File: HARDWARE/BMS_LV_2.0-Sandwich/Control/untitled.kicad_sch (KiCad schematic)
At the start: 14 parts, among them IC2 M24M02E-UFMN6TP, U1 STM32G484RETx, Y1 ATX-11-F-32.000MHZ-F05-T

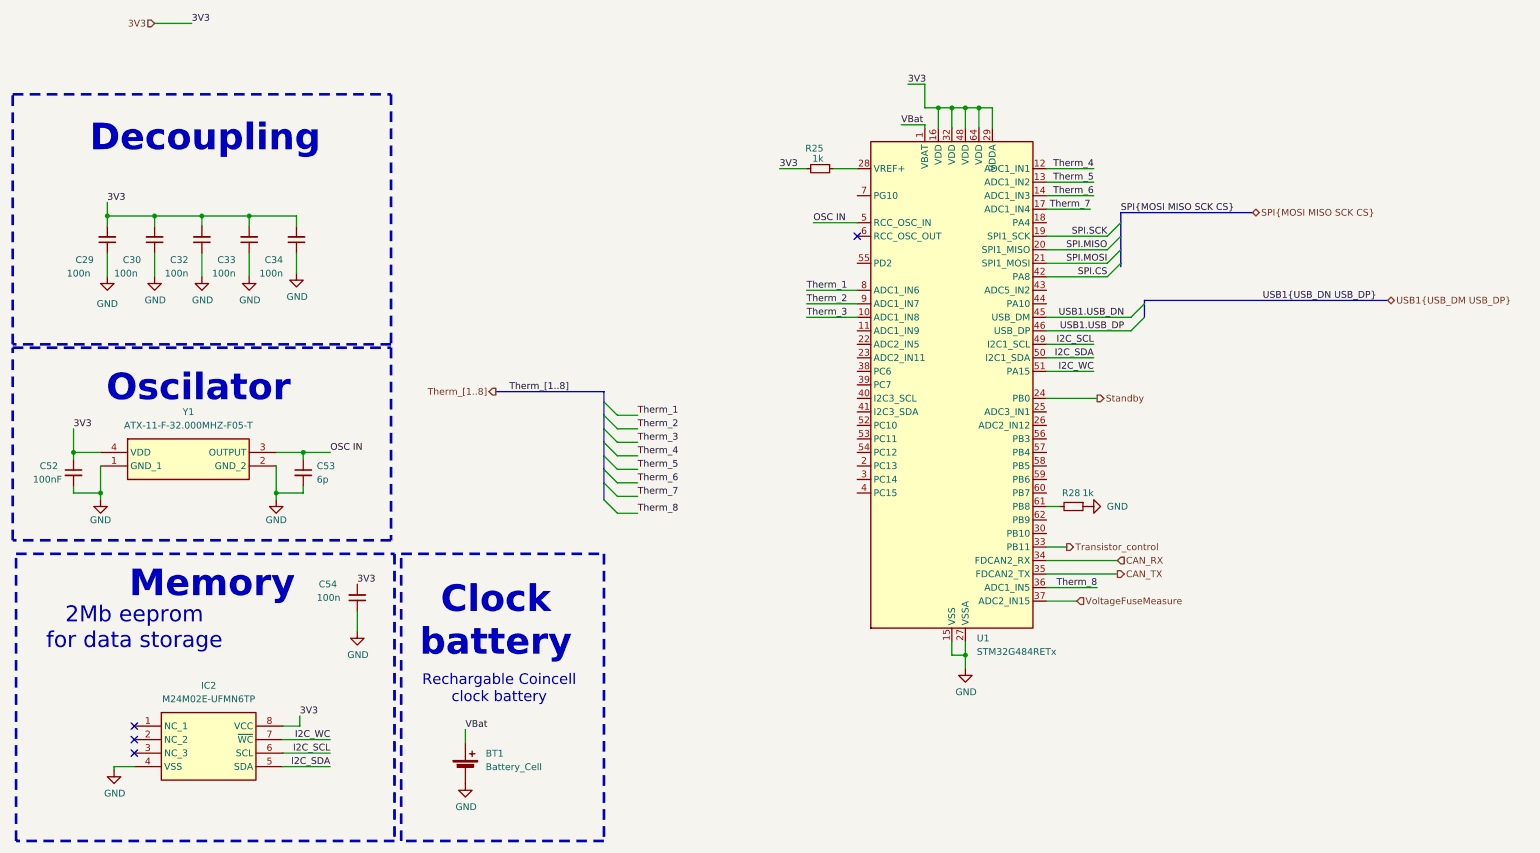
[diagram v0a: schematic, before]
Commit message: Zmiany w power: nowe bezpieczniki, nowy wymienialny layout dla tych bezpiecznikow, dodano diode zenera dla stabilizacji napięcia, zmiany dla control:  wyjebany eeprom, przesunięty can, zmieniony layout przetwornic, dodano programator i tvs, jeszcze do dokonczenia routing w control.
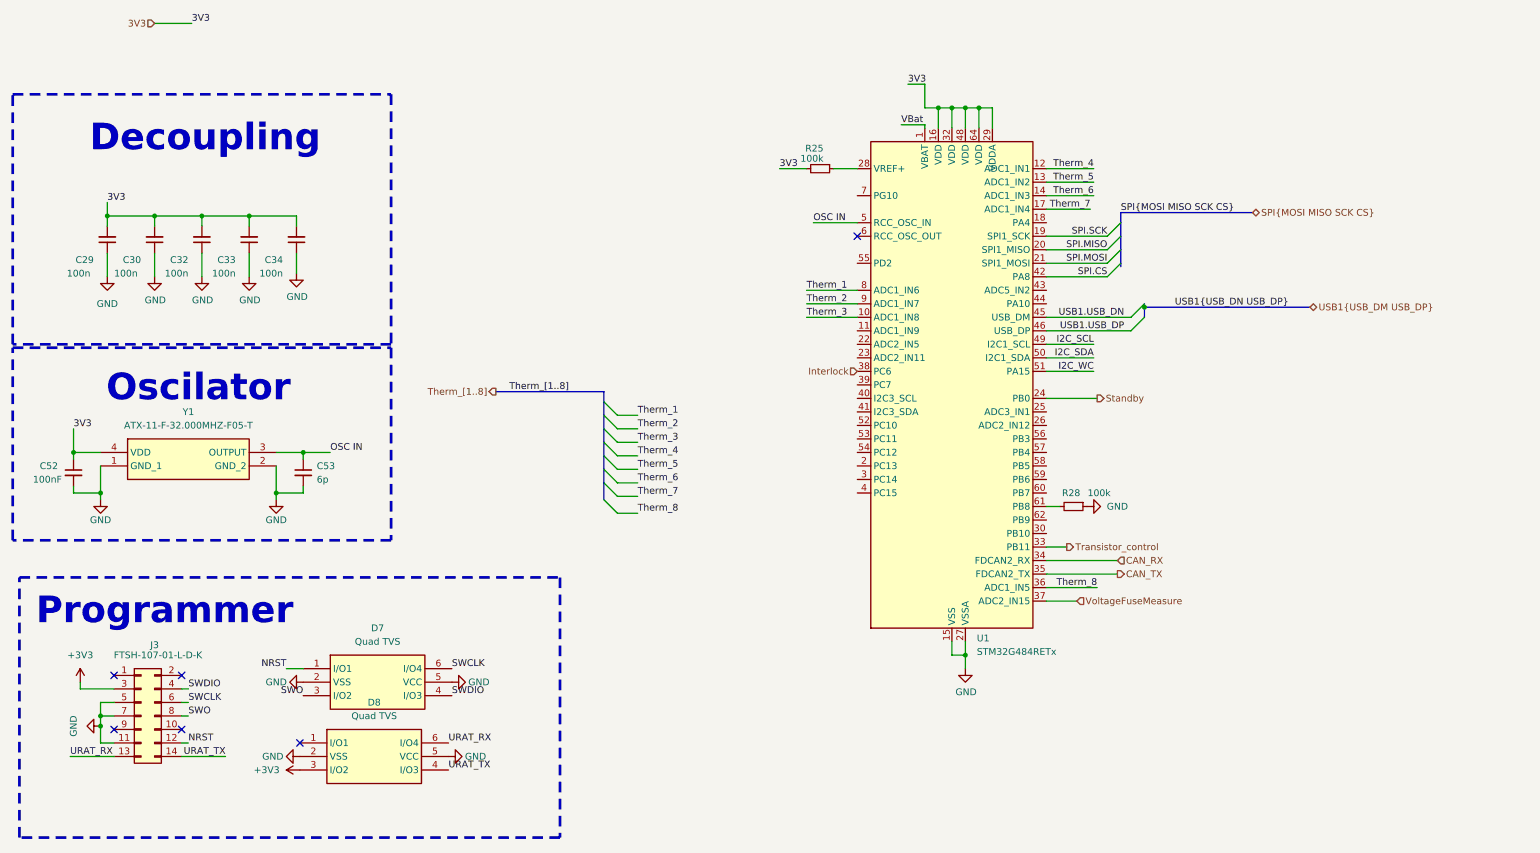
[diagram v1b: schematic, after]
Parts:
- removed BT1: Battery_Cell, Footprint:BATHLD001, symbol Device:Battery_Cell
- removed C54: 100n, Capacitor_SMD:C_0603_1608Metric_Pad1.08x0.95mm_HandSolder, symbol Device:C_Small
- removed IC2: M24M02E-UFMN6TP, SOIC127P600X175-8N, symbol M24M02E-UFMN6TP:M24M02E-UFMN6TP
- added D7, D8: Quad TVS, SOT95P285X140-6N, symbol D5V0P4UR6SO-7:D5V0P4UR6SO-7
- added J3: FTSH-107-01-L-D-K, Footprint:FTSH-107-XX-YYY-DV-K, symbol Samacsys_kicad_sym:FTSH-107-01-L-D-K
- R25, R28: value 1k -> 100k
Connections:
- net GND: now also D7.2 (VSS), D7.5 (VCC), D8.2 (VSS), D8.5 (VCC), J3.11 (Pin_11), J3.5 (Pin_5), J3.7 (Pin_7)
- net Interlock: now reaches U1.38 (PC6)
- new net +3V3: D8.3 (I/O2), J3.3 (Pin_3)
- new net NRST: D7.1 (I/O1), J3.12 (Pin_12)
- new net SWCLK: D7.6 (I/O4), J3.6 (Pin_6)
- new net SWDIO: D7.4 (I/O3), J3.4 (Pin_4)
- new net SWO: D7.3 (I/O2), J3.8 (Pin_8)
- new net URAT_RX: D8.6 (I/O4), J3.13 (Pin_13)
- new net URAT_TX: D8.4 (I/O3), J3.14 (Pin_14)
- no-connect marks 4 -> 6
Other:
- note added: "Programmer"
- note removed: "2Mb eeprom for data storage"
- note removed: "Clock battery"
- note removed: "Memory"
- note removed: "Rechargable Coincell clock battery"

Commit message: Routing 65%
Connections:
- net I2C_SCL is gone; now on net SWDIO: U1.49 (PA13)
- net I2C_SDA is gone; now on net SWCLK: U1.50 (PA14)
- net +3V3: no longer D8.3 (I/O2)
- net 3V3: now also D8.3 (I/O2)
- net NRST: now also R28.2, U1.61 (PB8)
- net SWCLK: now also D7.4 (I/O3); no longer D7.6 (I/O4)
- net SWDIO: now also D7.6 (I/O4); no longer D7.4 (I/O3)
- net Therm_1: now also U1.12 (PA0); no longer U1.8 (PC0)
- net Therm_2: now also U1.13 (PA1); no longer U1.9 (PC1)
- net Therm_3: now also U1.14 (PA2); no longer U1.10 (PC2)
- net Therm_4: now also U1.17 (PA3); no longer U1.12 (PA0)
- net Therm_5: now also U1.36 (PB14); no longer U1.13 (PA1)
- net Therm_6: no longer U1.14 (PA2)
- net Therm_7: now also U1.9 (PC1); no longer U1.17 (PA3)
- net Therm_8: now also U1.10 (PC2), U1.8 (PC0); no longer U1.36 (PB14)
- net URAT_RX: now also D8.4 (I/O3), U1.52 (PC10); no longer D8.6 (I/O4)
- net URAT_TX: now also D8.6 (I/O4), U1.53 (PC11); no longer D8.4 (I/O3)
- net I2C_WC: no longer names the net of U1.51 (PA15)
- no-connect marks 6 -> 7
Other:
- moved on the sheet: R28

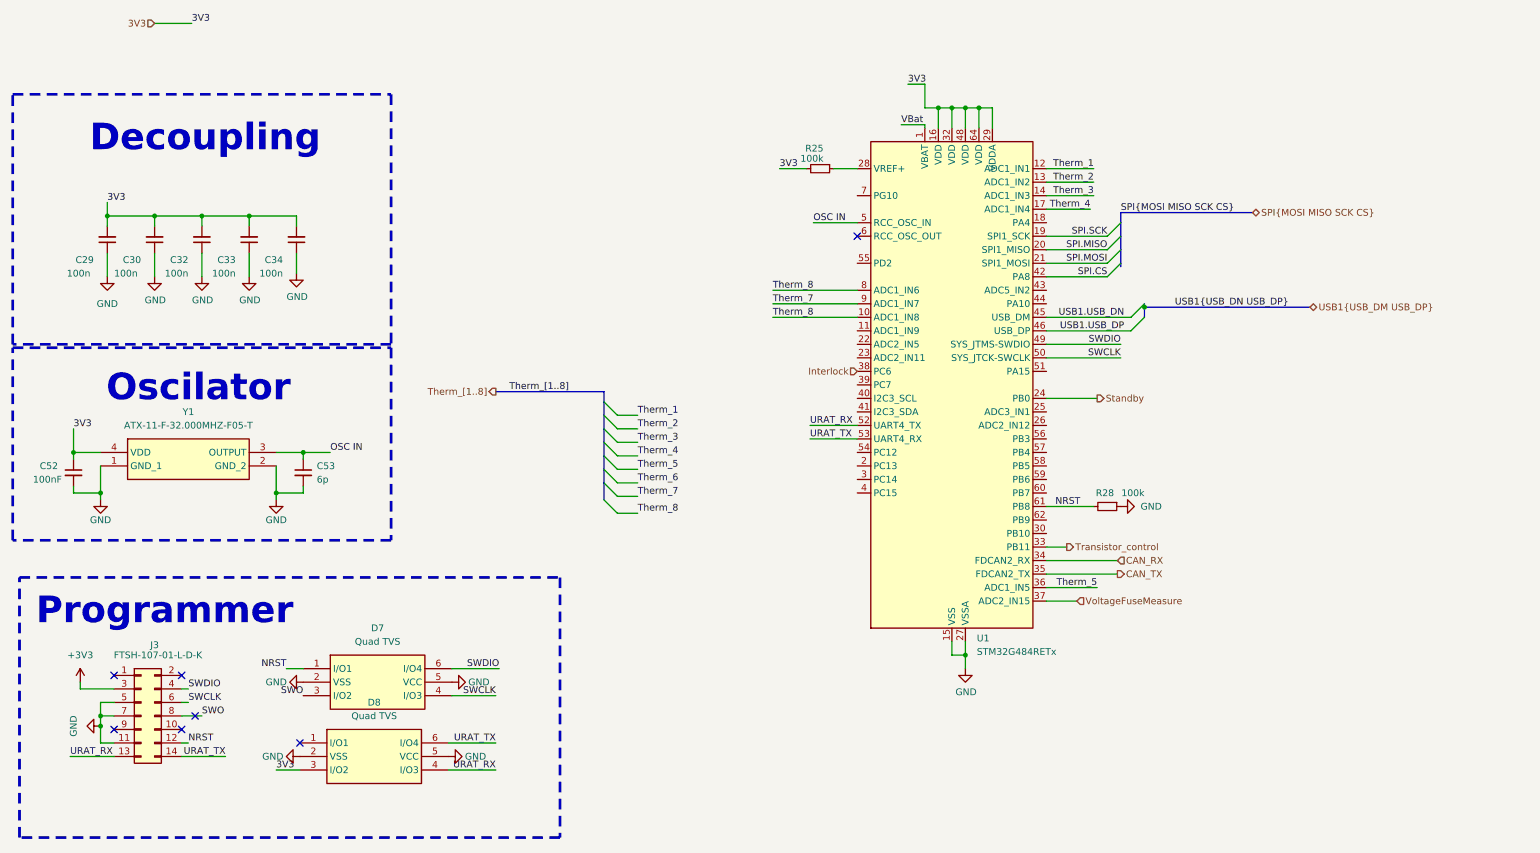
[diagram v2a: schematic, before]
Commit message: Pierwsza wersja bez błędów DRC/ERC, skończony routing plytki control
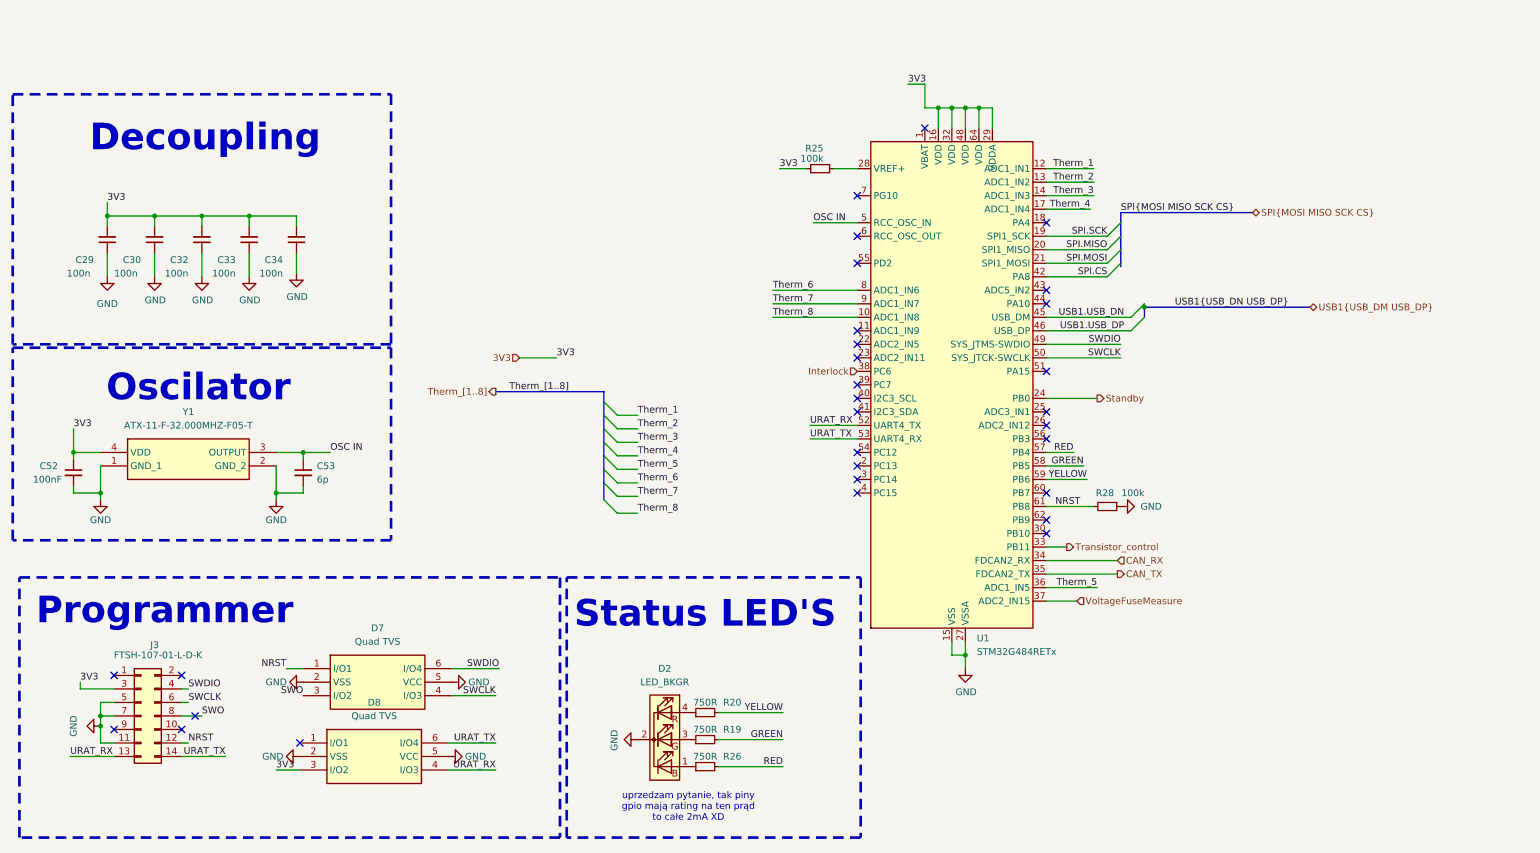
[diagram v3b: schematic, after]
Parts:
- added D2: LED_BKGR, Footprint:APFA2507LSURKSYKZGKC, symbol Device:LED_BKGR
- added R19, R20, R26: 750R, Resistor_SMD:R_0603_1608Metric_Pad0.98x0.95mm_HandSolder, symbol Device:R_Small
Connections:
- net +3V3 is gone; now on net 3V3: J3.3 (Pin_3)
- net GND: now also D2.2 (K)
- net Therm_6: now also U1.8 (PC0)
- net Therm_8: no longer U1.8 (PC0)
- net RED: now reaches U1.57 (PB4)
- net RED: now also R26.2
- net GREEN: now reaches U1.58 (PB5)
- net GREEN: now also R19.2
- net YELLOW: now reaches U1.59 (PB6)
- net YELLOW: now also R20.2
- net VBat: no longer names the net of U1.1 (VBAT)
- new net: D2.1 (BA), R26.1
- new net: D2.3 (GA), R19.1
- new net: D2.4 (RA), R20.1
- no-connect marks 7 -> 30
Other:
- note added: "Status LED'S"
- note added: "uprzedzam pytanie, tak piny gpio mają rating na ten prąd to całe 2mA XD"

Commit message: Ulozono silkscreena
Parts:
- removed C33: 100n, Capacitor_SMD:C_0603_1608Metric_Pad1.08x0.95mm_HandSolder, symbol Device:C_Small
- added C60, C61: 100n, Capacitor_SMD:C_0603_1608Metric_Pad1.08x0.95mm_HandSolder, symbol Device:C_Small
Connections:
- net 3V3: no longer R25.2, U1.29 (VDDA)
- net GND: now also C60.1, C61.1
- net NRST: now also U1.7 (PG10); no longer R28.2, U1.61 (PB8)
- net SWCLK: now also D7.6 (I/O4); no longer D7.4 (I/O3)
- net SWDIO: now also D7.4 (I/O3); no longer D7.6 (I/O4)
- net SWO: no longer D7.3 (I/O2)
- net Therm_4: now also U1.8 (PC0); no longer U1.17 (PA3)
- net Therm_5: now also U1.9 (PC1); no longer U1.36 (PB14)
- net Therm_6: now also U1.10 (PC2); no longer U1.8 (PC0)
- net Therm_7: now also U1.17 (PA3); no longer U1.9 (PC1)
- net Therm_8: now also U1.36 (PB14); no longer U1.10 (PC2)
- new net: R28.2, U1.61 (PB8)
- new net 3V3A: C60.2, C61.2, R25.2, U1.29 (VDDA)
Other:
- moved on the sheet: C29, C30, C32, C34

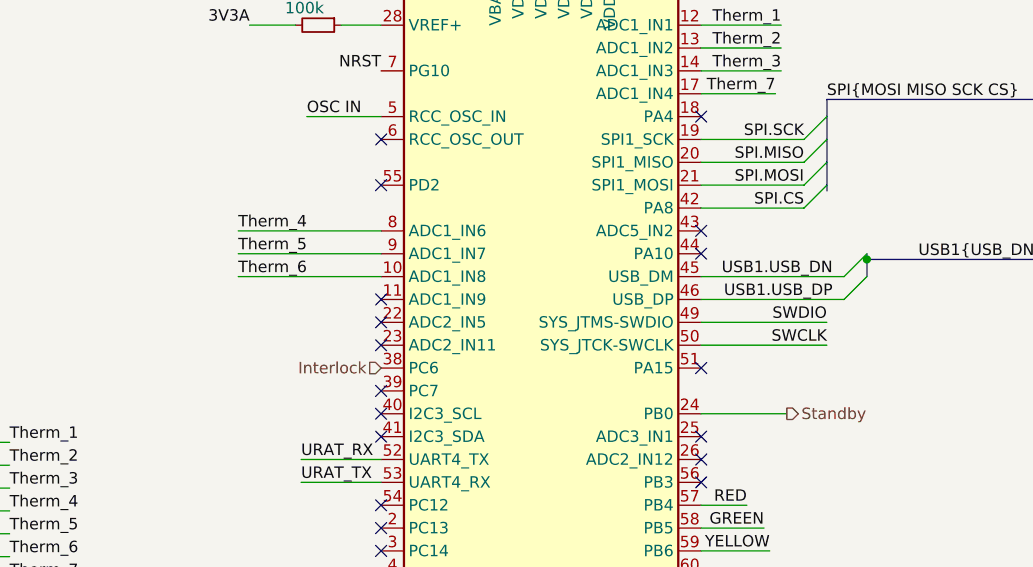
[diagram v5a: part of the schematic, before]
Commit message: Naprawiono: załączanie lv, brak zlącza programatora (XD) oraz brak podłączenia czujnika prądu :9
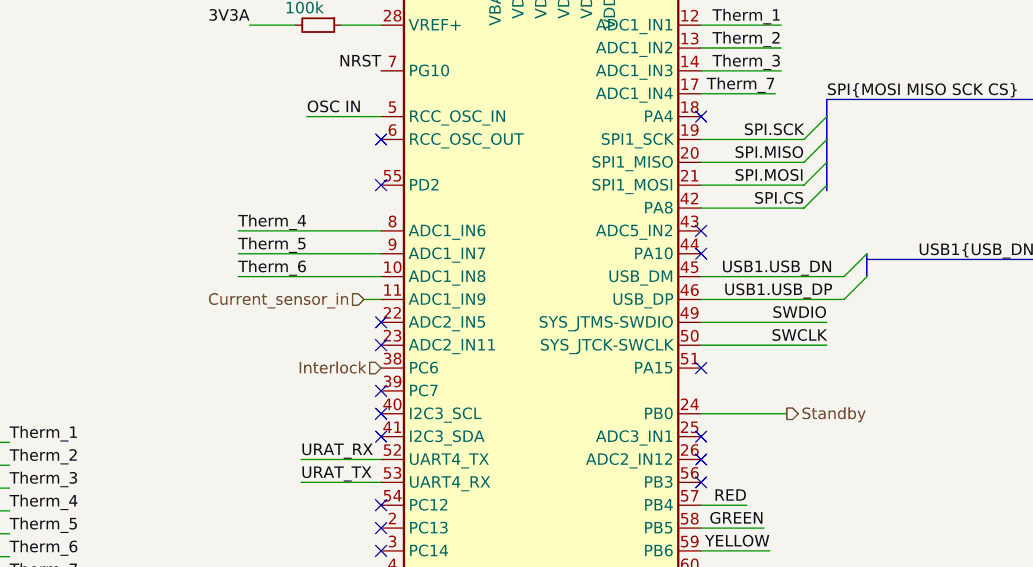
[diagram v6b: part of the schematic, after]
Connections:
- net Current_sensor_in: now reaches U1.11 (PC3)
- no-connect marks 30 -> 29
